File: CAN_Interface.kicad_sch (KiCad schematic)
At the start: 9 parts, among them CN2 BM04B-ACHSS, U8 TCAN1057AVDRBRQ1

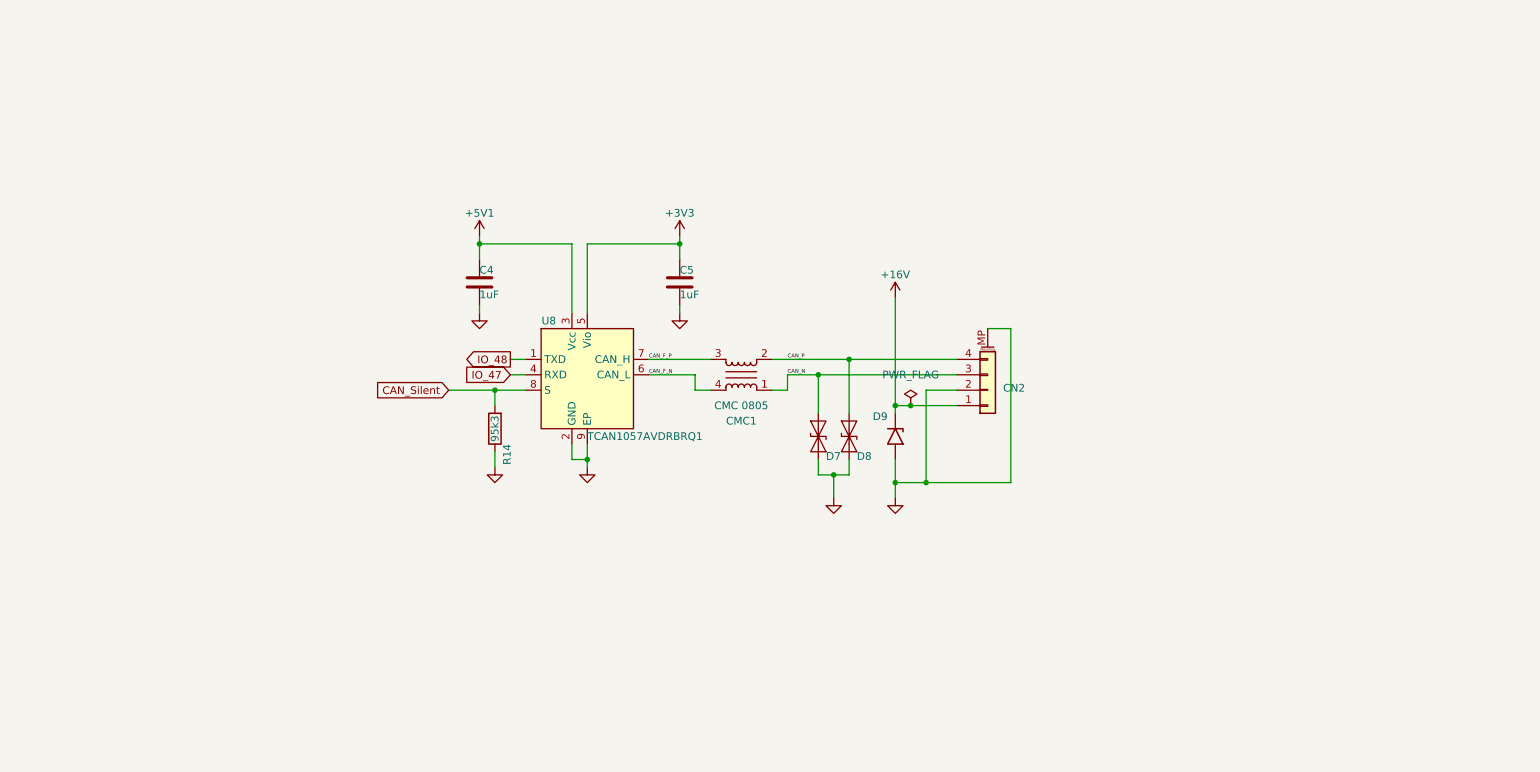
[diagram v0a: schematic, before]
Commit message: streamlined routing by discarding legacy GPIO pinout compatibility. reduced Vin to Vcc and Vbus (no more +16V) includes CAN & Vehicle inputs (need to move to 2nd board, though) added wake-on-start by wiring Vacc to RTC_IO
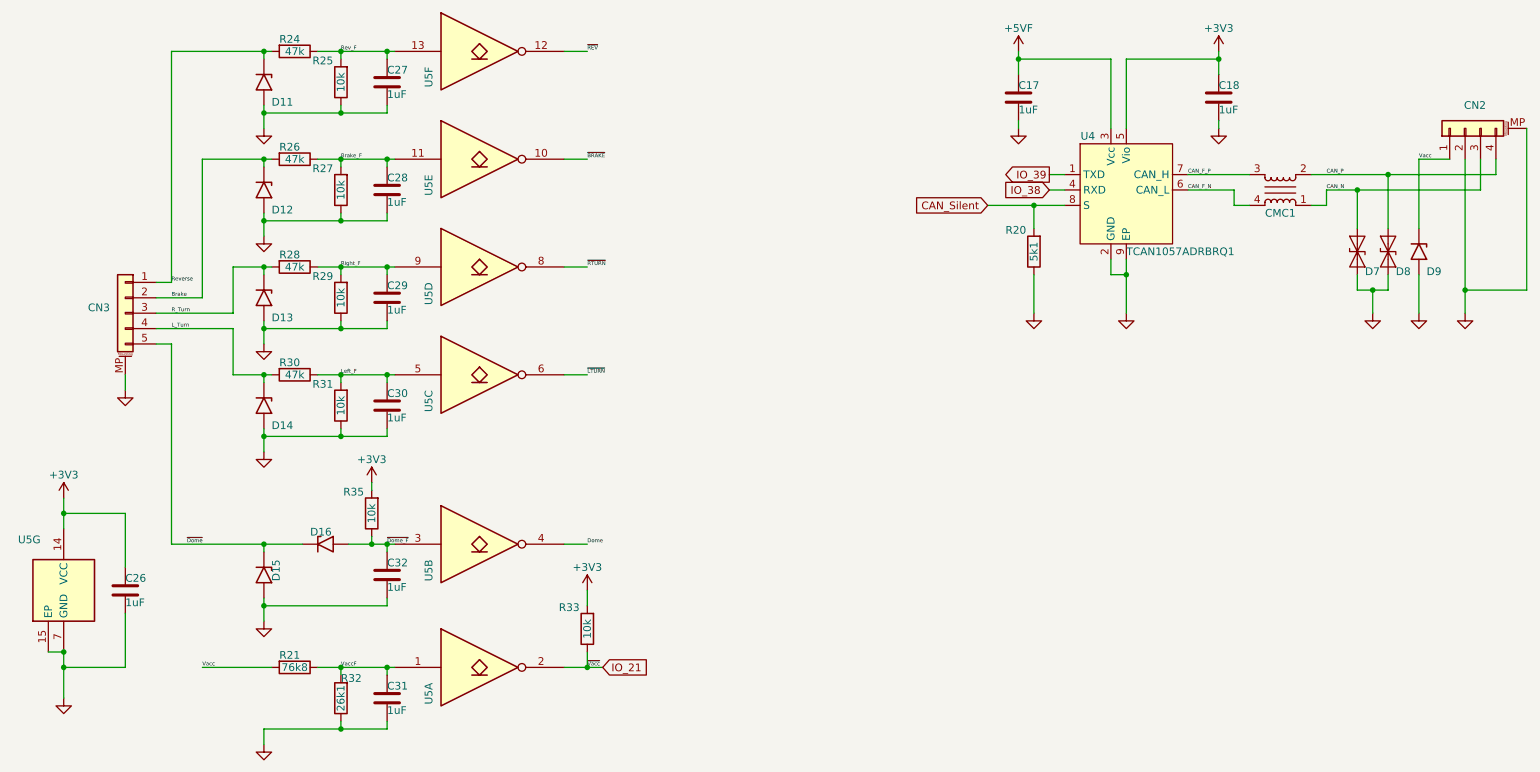
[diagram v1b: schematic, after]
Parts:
- removed C4, C5: 1uF, Capacitors:C0201_Dense, symbol Device:C
- removed CN2: BM04B-ACHSS, Personal_FootprintLibrary:JST_ACH_BM04B-ACHSS-A-GAN-ETF_1x04-1MP_P1.20mm_Vertical, symbol Connector_Generic_MountingPin:Conn_01x04_MountingPin
- removed R14: 95k3, Resistors:R0201_Dense, symbol Device:R
- added C17, C18, C26, C27, C28, C29, C30, C31, C32: 1uF, Capacitors:C_0201_Dense, symbol Device:C
- added CN2: SM04B-SURS-TF(LF)(SN), Personal_FootprintLibrary:JST_SUH_1x04_MP_P0.8mm, symbol PersonalSchematicSymbolLibrary:Conn_01x04_MountingPin
- added CN3: SM05B-SURS-TF(LF)(SN), Personal_FootprintLibrary:JST_SUH_1x05_MP_P0.8mm, symbol PersonalSchematicSymbolLibrary:Conn_01x05_MountingPin
- added D11, D12, D13, D14, D15, D16: D15V0H1U2LP-7B, Personal_FootprintLibrary:DFN1006-2, symbol PersonalSchematicSymbolLibrary:TVS_Unidirectional
- added R20: 5k1, Resistors:R_0201_Dense, symbol Device:R
- added R21: 76k8, Resistors:R_0201_Dense, symbol Device:R
- added R24, R26, R28, R30: 47k, Resistors:R_0201_Dense, symbol Device:R
- added R25, R27, R29, R31, R33, R35: 10k, Resistors:R_0201_Dense, symbol Device:R
- added R32: 26k1, Resistors:R_0201_Dense, symbol Device:R
- added U5: 74LVC06A, Personal_FootprintLibrary:DHVQFN-14-1EP_2.5x3mm_P0.5mm_EP1x1.5mm, symbol PersonalSchematicSymbolLibrary:74LVC06
- CMC1: Distributor LInk 1 https://www.digikey.com/en/products/detail/tdk-corporation/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 -> (none); Distributor Link 1 (none) -> https://www.digikey.com/en/products/detail/tdk-corporation/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
- D7, D8: value ESDSLC24VLB-TP -> SZESD7241N2T5G; Distributor Link 1 https://www.digikey.com/en/products/detail/mcc-micro-commer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 -> https://www.digikey.com/en/products/detail/onsemi/SZESD7241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; Distributor Link 2 https://www.mouser.com/ProductDetail/Micro-Commercial-Compo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 -> https://www.mouser.com/ProductDetail/onsemi/SZESD7241N2T5G?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; LCSC C7463931 -> C604770; Manufacturer MCC(Micro Commercial Components) -> onsemi; Manufacturer Part Number ESDSLC24VLB-TP -> SZESD7241N2T5G
- U4: renamed from U8; footprint Personal_FootprintLibrary:VSON-8-1EP_3x3mm_P0.65mm_EP1.65x2.4mm_ThermalVias -> Personal_FootprintLibrary:VSON-8-1EP_3x3mm_P0.65mm_EP1.65x2.4mm; Distributor Link 1 https://www.digikey.com/en/products/detail/texas-instruments/TCAN1057AVDRBRQ1/15857376 -> https://www.digikey.com/en/products/detail/texas-instruments/TCAN1057ADRBRQ1/18159080; Distributor Link 2 https://www.mouser.com/ProductDetail/Texas-Instruments/TCAN1057AVDRBRQ1?qs=pBJMDPsKWf3H7%2FKJZPMbcg%3D%3D -> https://www.mouser.com/ProductDetail/Texas-Instruments/TCAN1057ADRBRQ1?qs=doiCPypUmgEnlQZgkBC9zw%3D%3D; LCSC C3234121 -> C5215844; Manufacturer Part Number TCAN1057AVDRBRQ1 -> TCAN1057ADRBRQ1
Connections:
- net +3V3: now also C18.1, C26.1, R33.2, R35.2, U5.14 (VCC)
- net CAN_N: now also CN2.3 (Pin_3)
- net CAN_P: now also CN2.4 (Pin_4)
- net CAN_Silent: now also R20.2
- net GND: now also C17.2, C18.2, C26.2, C27.2, C28.2, C29.2, C30.2, C31.2, C32.2, CN2.2 (Pin_2), CN2.MP (MountPin), CN3.MP (MountPin), D11.2 (A), D12.2 (A), D13.2 (A), D14.2 (A), D15.2 (A), R20.1, R25.1, R27.1, R29.1, R31.1, R32.1, U5.15 (EP), U5.7 (GND)
- net +16V renamed Vacc
- net Vacc: now also CN2.1 (Pin_1), R21.2
- net +5V1 renamed +5VF
- net +5VF: now also C17.1
- net IO_47 renamed IO_38
- net IO_48 renamed IO_39
- new net Brake: CN3.2 (Pin_2), D12.1 (K), R26.2
- new net Brake_F: C28.1, R26.1, R27.2, U5.11
- new net Dome: U5.4
- new net IO_21: R33.1, U5.2
- new net L_Turn: CN3.4 (Pin_4), D14.1 (K), R30.2
- new net Left_F: C30.1, R30.1, R31.2, U5.5
- new net R_Turn: CN3.3 (Pin_3), D13.1 (K), R28.2
- new net Rev_F: C27.1, R24.1, R25.2, U5.13
- new net Reverse: CN3.1 (Pin_1), D11.1 (K), R24.2
- new net Right_F: C29.1, R28.1, R29.2, U5.9
- new net VaccF: C31.1, R21.1, R32.2, U5.1
- new net ~{BRAKE}: U5.10
- new net ~{Dome_F}: C32.1, D16.2 (A), R35.1, U5.3
- new net ~{Dome}: CN3.5 (Pin_5), D15.1 (K), D16.1 (K)
- new net ~{LTURN}: U5.6
- new net ~{REV}: U5.12
- new net ~{RTURN}: U5.8
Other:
- moved on the sheet: CMC1, D7, U4
